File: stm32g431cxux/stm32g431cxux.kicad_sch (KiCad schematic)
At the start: 23 parts, among them J1 USB2.0_C_v3, J2 ProMicro-LeftPin-NoGND, J3 ProMicro-RightPin, SW1 SW_Push, U1 AMS1117-3.3, U2 STM32G431CBUx, Y1 24M

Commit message: before free routing
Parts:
- removed C7, C8: 12p, $74th:Capacitor_0603_1608, symbol Device:C
- removed Y1: 24M, $74th:Crystal_SMD_3225-4Pin_3.2x2.5mm_HandSoldering, symbol $74th:Oscillator_24GND
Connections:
- net SWD_CLK is gone; now on net SWCLK: CH1.6 (SWCLK)
- net SWD_DIO is gone; now on net SWDIO: CH1.1 (SWDIO)
- net 0/UART_RX: now also CH1.3 (TXD); no longer CH1.5 (RXD)
- net 1/UART_TX: now also CH1.5 (RXD); no longer CH1.3 (TXD)
- no-connect marks 16 -> 18

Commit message: stm32g03xfxp/v1.3.0
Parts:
- removed CH1: DAPLink-SWD-Recv-6Pin, $74th:BoxPinHeader_2x03_P1.27mm_Vertical, symbol $74th:DAPLink-SWD-Recv-6Pin
- added J2: SWD-MCU_Side-10Pin, $74th:SWD_2x05_P1.27mm, symbol $74th:SWD-MCU_Side-10Pin
- U1: footprint $74th:Regulator_AMS1117_SOT-89 -> Package_TO_SOT_SMD:SOT-89-3_Handsoldering
- U2: footprint Package_DFN_QFN:QFN-48-1EP_7x7mm_P0.5mm_EP5.6x5.6mm -> $74th:QFN-48-1EP_7x7mm_P0.5mm_EP5.6x5.6mm
- renumbered C2 to C1, C1 to C2, C6 to C3, C5 to C4, C4 to C5, C3 to C6, J2 to J3, J3 to J4, R2 to R1, R1 to R2
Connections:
- net +3V3: now also J2.1 (VCC)
- net 0/UART_RX: now also J2.7 (RXD)
- net 10/A10: now also U2.8 (PA0); no longer U2.47 (PB9)
- net 18/A0: now also U2.9 (PA1); no longer U2.10 (PA2)
- net 19/A1: now also U2.10 (PA2); no longer U2.11 (PA3)
- net 1/UART_TX: now also J2.8 (TXD)
- net 20/A2: now also U2.11 (PA3); no longer U2.38 (PA15)
- net 4/A6: now also U2.32 (PA10); no longer U2.8 (PA0)
- net 5: now also U2.38 (PA15); no longer U2.43 (PB5)
- net 6/A7: now also U2.42 (PB4); no longer U2.9 (PA1)
- net 7: now also U2.47 (PB9); no longer U2.32 (PA10)
- net 8/A9: now also U2.6 (PF1); no longer U2.41 (PB3)
- net 9/A9: now also U2.5 (PF0); no longer U2.42 (PB4)
- net GND: now also J2.3 (GND), J2.5 (GND), J2.9 (GND)
- net NRST: now also J2.10 (~{RESET})
- net SWCLK: now also J2.4 (SWCLK)
- net SWDIO: now also J2.2 (SWDIO)
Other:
- moved on the sheet: R4

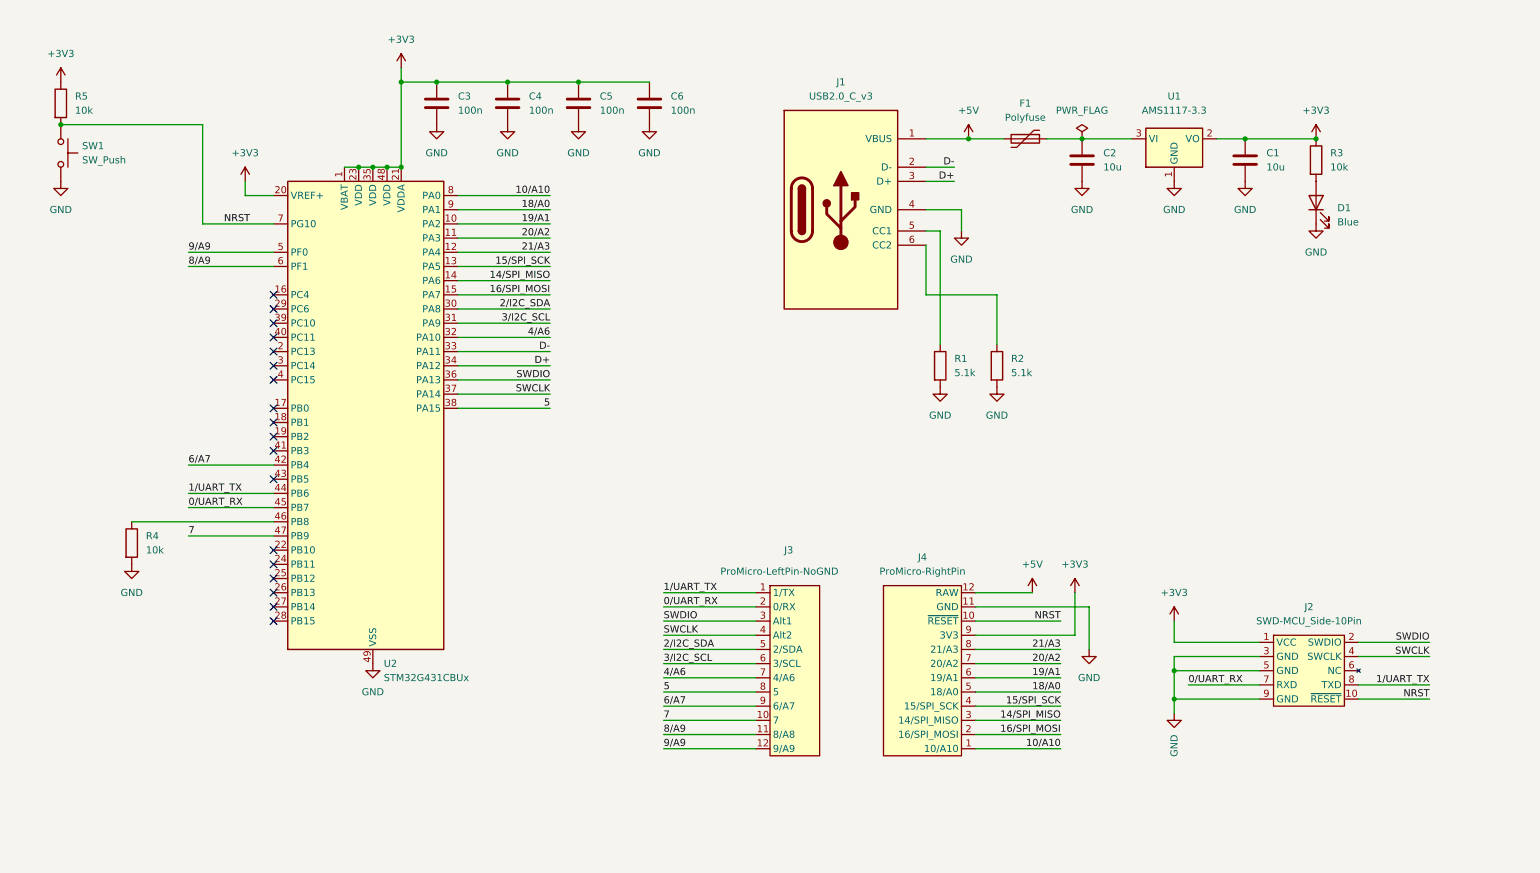
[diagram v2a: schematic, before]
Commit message: update semantics
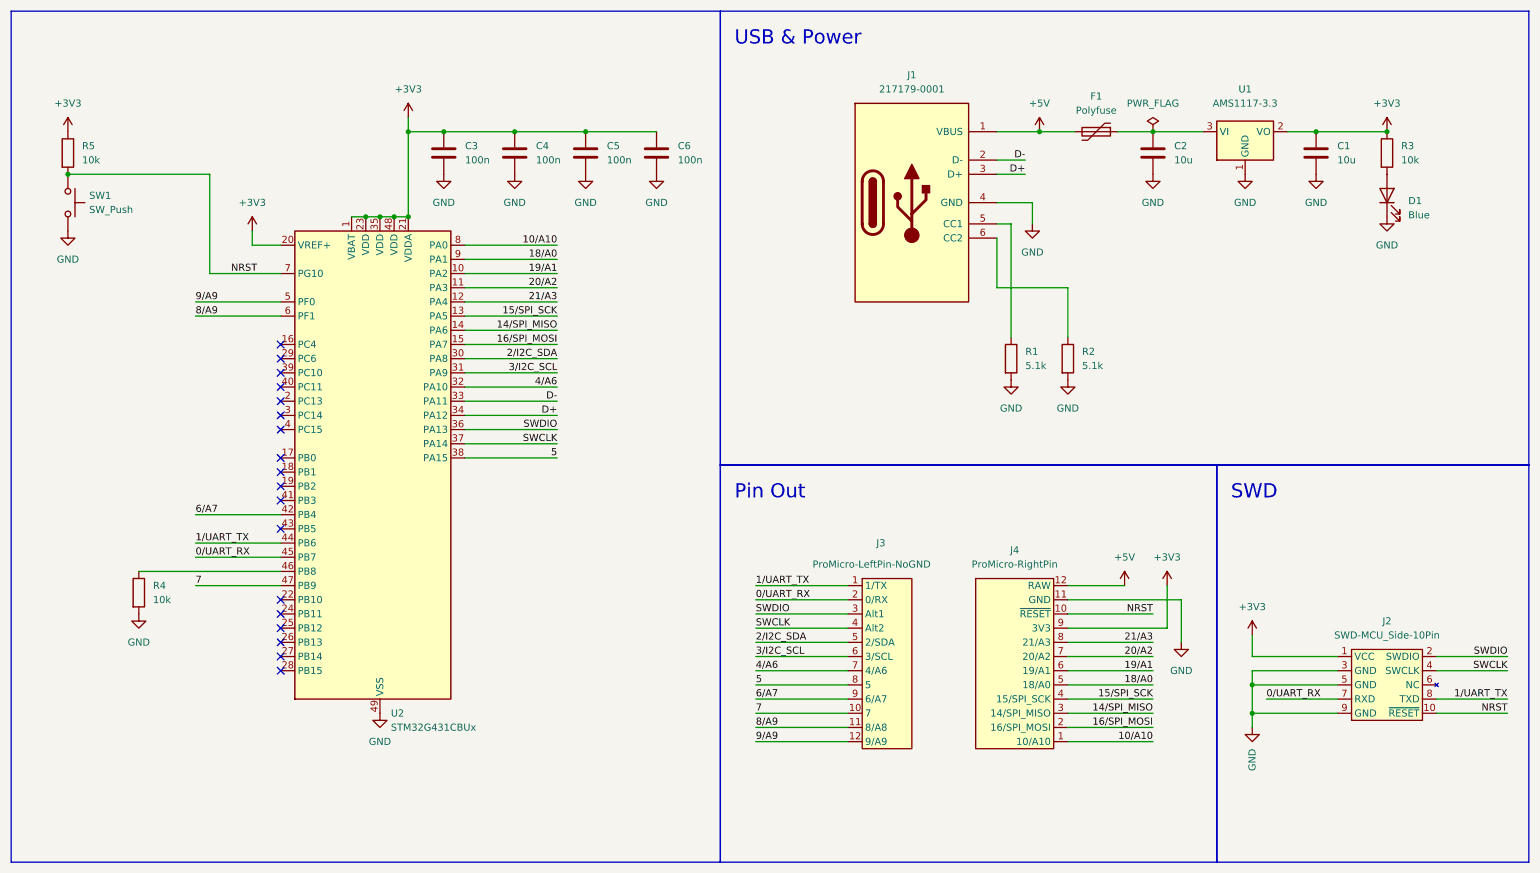
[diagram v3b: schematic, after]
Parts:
- J1: value USB2.0_C_v3 -> 217179-0001
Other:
- note added: "Pin Out"
- note added: "SWD"
- note added: "USB & Power"
- company: (none) -> 74th
- title: (none) -> STM32G431 ProMicro
- moved on the sheet: C1, C2, C3, C4, C5, C6, D1, F1, J1, J2, J3, J4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
